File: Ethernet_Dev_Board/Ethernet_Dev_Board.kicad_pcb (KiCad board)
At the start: 2 copper layers, 123 parts, among them J102 5V, J103 3.3V, J104 3.3VA, J105 3.3VD, J401 TAG-CONNECT_NL_10-POS_LEGS, Q201 PMV48XPA2R, Q401 PMV48XPA2R, Q402 PMV48XPA2R, U101 AZ1117, U201 WIZNET_W5500, U202 74AUP1T08GWH, U302 74AUP1T08GWH, U401 74AUP1T08GWH, U402 ESP32-WROOM-32E

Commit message: Added in 1.2 V regulator and broke out unused IO pins to header
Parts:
- removed Q401, Q402: PMV48XPA2R, RG_TO_SOT_SMD:SOT23-3P95
- removed R404, R405: 10k, RG_Resistors_SMD:0603
- added J101: Power In, RG_Terminals:CUI_TBP01R1-508-02BE, F.Cu at (57.2, 49.2)
- added TVS101: 3.3V, RG_Diode:SMB-D, F.Cu at (71.8, 41.3)
- added TVS102: 3.3V, RG_Diode:SMB-D, F.Cu at (71.8, 46.6)
- added Y201: 25MHz, RG_Crystal:Crystal_SMD_4Pin_7.0mmx5.0mm, F.Cu at (47.4, 57.0)
- added Y301: 25MHz, RG_Crystal:Crystal_SMD_4Pin_3.2x2.5mm, F.Cu at (67.0, 56.0)
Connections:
- LED401 pad C: GNDS -> Net-(U402-IO16)
- LED402 pad C: GNDS -> Net-(U402-IO22)
- R406 pad 2: Net-(Q401-D) -> +3.3V
- R407 pad 2: Net-(Q402-D) -> +3.3V
- U402 pad 27: Net-(Q401-G) -> Net-(U402-IO16)
- U402 pad 36: Net-(Q402-G) -> Net-(U402-IO22)

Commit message: Net adjustments. Beginning board layout
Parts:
- removed J102: 5V, RG_Terminals:PAD_0.0638
- removed J103: 3.3V, RG_Terminals:PAD_0.0638
- removed J104: 3.3VA, RG_Terminals:PAD_0.0638
- removed J105: 3.3VD, RG_Terminals:PAD_0.0638
- added C114: 0.1uF, RG_Capacitors_SMD:0603, F.Cu at (98.6, 63.5)
- added C116: 1uF, RG_Capacitors_SMD:0603, F.Cu at (98.6, 66.1)
- added J402: ~, Connector_PinHeader_2.54mm:PinHeader_1x14_P2.54mm_Vertical, F.Cu at (111.8, 47.0)
- added R404: 10k, RG_Resistors_SMD:0603, F.Cu at (64.3, 56.8)
- added U102: 1.2V, RG_TO_SOT_SMD:SOT23-5P65, F.Cu at (97.1, 58.8)
- LED101: value 5V Power -> Power
- LED201: value ACTLED -> 5500 ACT
- LED301: value ACTLED -> 5100 ACT
- LED401: renamed from LED402; value ETH Connected -> ETH
- LED402: renamed from LED401; value MQTT Connected -> MQTT
- moved R319 132.1 mm to (50.0, 98.4), turned to 90 degrees
- moved LED301 124.1 mm to (50.5, 101.6)
- moved R405 88.1 mm to (44.5, 98.5), turned to 90 degrees
- moved R406 86.1 mm to (47.2, 98.5), turned to 90 degrees
- moved Y201 84.9 mm to (123.2, 95.2)
- moved LED402 82.5 mm to (42.2, 106.7)
- moved LED401 81.2 mm to (42.2, 104.1)
- moved C117 80.8 mm to (147.3, 88.9), turned to 180 degrees
- moved R213 79.3 mm to (138.4, 74.9)
- moved R102 77.6 mm to (138.4, 78.7), turned to 180 degrees
- moved C115 77.3 mm to (138.4, 77.5), turned to 180 degrees
- moved C207 76.0 mm to (131.2, 82.5)
- moved S401 74.6 mm to (65.4, 103.8)
- moved D301 73.8 mm to (115.0, 36.8)
- moved C403 73.5 mm to (48.0, 80.2), turned to 180 degrees
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- renumbered C114 to C115, C115 to C117, R407 to R405
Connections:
- net Net-(R302-Pad2) renamed /W5100S_Dev/TX51_N
- net Net-(R303-Pad2) renamed /W5100S_Dev/TX51_P
- net Net-(R304-Pad2) renamed /W5100S_Dev/RX51_N
- net Net-(R305-Pad2) renamed /W5100S_Dev/RX51_P
- net Net-(U301-RXIN) renamed /W5100S_Dev/RXI_N
- net Net-(U301-RXIP) renamed /W5100S_Dev/RXI_P
- net Net-(U301-TXON) renamed /W5100S_Dev/TXO_N
- net Net-(U301-TXOP) renamed /W5100S_Dev/TXO_P
- net Net-(U401A-A) renamed /ESP32/ESP_RST
- net RXN renamed RX_N
- net RXN_ETH renamed ETH_RX_N
- net RXP renamed RX_P
- net RXP_ETH renamed ETH_RX_P
- net TXN renamed TX_N
- net TXN_ETH renamed ETH_TX_N
- net TXP renamed TX_P
- net TXP_ETH renamed ETH_TX_P
- C102 pad 2: GNDS -> GND1
- C103 pad 2: GNDS -> GND1
- C105 pad 2: GNDS -> GND1
- C106 pad 2: GNDS -> GND1
- C107 pad 2: GNDS -> GND1
- C108 pad 2: GNDS -> GND1
- C109 pad 2: GNDS -> GND1
- C110 pad 2: GNDS -> GND1
- C111 pad 2: GNDS -> GND1
- C112 pad 2: GNDS -> GND1
- C113 pad 2: GNDS -> GND1
- C115 pad 2: GNDS -> GND1
- C117 pad 2: GNDS -> GND1
- C201 pad 2: GNDS -> GND1
- C202 pad 2: GNDS -> GND1
- C203 pad 2: GNDS -> GND1
- C204 pad 2: GNDS -> GND1
- C205 pad 2: GNDS -> GND1
- C206 pad 2: GNDS -> GND1
- C209 pad 2: GNDS -> GND1
- C210 pad 2: GNDS -> GND1
- C301 pad 2: GNDS -> GND1
- C302 pad 1: +1.2VO -> +1.2V
- C302 pad 2: GNDS -> GND1
- C303 pad 2: GNDS -> GND1
- C304 pad 2: GNDS -> GND1
- C305 pad 2: GNDS -> GND1
- C306 pad 2: GNDS -> GND1
- C307 pad 2: GNDS -> GND1
- C308 pad 2: GNDS -> GND1
- C309 pad 2: GNDS -> GND1
- C310 pad 2: GNDS -> GND1
- C311 pad 2: GNDS -> GND1
- C312 pad 2: GNDS -> GND1
- C313 pad 2: GNDS -> GND1
- C401 pad 2: GNDS -> GND1
- C402 pad 2: GNDS -> GND1
- C403 pad 2: GNDS -> GND1
- C404 pad 2: GNDS -> GND1
- C405 pad 2: GNDS -> GND1
- C406 pad 2: GNDS -> GND1
- J401 pad 10: GNDS -> GND1
- LED402 pad C: Net-(U402-IO16) -> Net-(U402-IO17)
- R201 pad 2: GNDS -> GND1
- R202 pad 10: GNDS -> GND1
- R204 pad 1: GNDS -> GND1
- R301 pad 1: +1.2VO -> +1.2V
- R318 pad 1: GNDS -> GND1
- S401 pad 2: GNDS -> GND1
- S401 pad 4: GNDS -> GND1
- S402 pad 2: GNDS -> GND1
- S402 pad 4: GNDS -> GND1
- TVS101 pad A: GNDS -> GND1
- TVS102 pad A: GNDS -> GND1
- U201 pad 14: GNDS -> GND1
- U201 pad 16: GNDS -> GND1
- U201 pad 19: GNDS -> GND1
- U201 pad 29: GNDS -> GND1
- U201 pad 3: GNDS -> GND1
- U201 pad 48: GNDS -> GND1
- U201 pad 9: GNDS -> GND1
- U202 pad 3: GNDS -> GND1
- U301 pad 1: GNDS -> GND1
- U301 pad 10: GNDS -> GND1
- U301 pad 23: GNDS -> GND1
- U301 pad 25: GNDS -> GND1
- U301 pad 26: GNDS -> GND1
- U301 pad 27: GNDS -> GND1
- U301 pad 28: GNDS -> GND1
- U301 pad 46: GNDS -> GND1
- U301 pad 7: GNDS -> GND1
- U302 pad 3: GNDS -> GND1
- U401 pad 3: GNDS -> GND1
- U402 pad 1: GNDS -> GND1
- U402 pad 10: unconnected-(U402-IO25-Pad10) -> IO25
- U402 pad 11: unconnected-(U402-IO26-Pad11) -> IO26
- U402 pad 12: unconnected-(U402-IO27-Pad12) -> IO27
- U402 pad 13: unconnected-(U402-IO14-Pad13) -> IO14
- U402 pad 14: unconnected-(U402-IO12-Pad14) -> IO12
- U402 pad 15: GNDS -> GND1
- U402 pad 16: unconnected-(U402-IO13-Pad16) -> IO3
- U402 pad 23: unconnected-(U402-IO15-Pad23) -> IO5
- U402 pad 24: unconnected-(U402-IO2-Pad24) -> IO2
- U402 pad 28: unconnected-(U402-IO17-Pad28) -> Net-(U402-IO17)
- U402 pad 29: unconnected-(U402-IO5-Pad29) -> IO5
- U402 pad 33: unconnected-(U402-IO21-Pad33) -> IO21
- U402 pad 38: GNDS -> GND1
- U402 pad 39: GNDS -> GND1
- U402 pad 8: unconnected-(U402-IO32-Pad8) -> IO32
- U402 pad 9: unconnected-(U402-IO33-Pad9) -> IO33
- Y201 pad 2: GNDS -> GND1
- Y301 pad 2: GNDS -> GND1
- Y301 pad 4: +1.2VO -> +1.2V

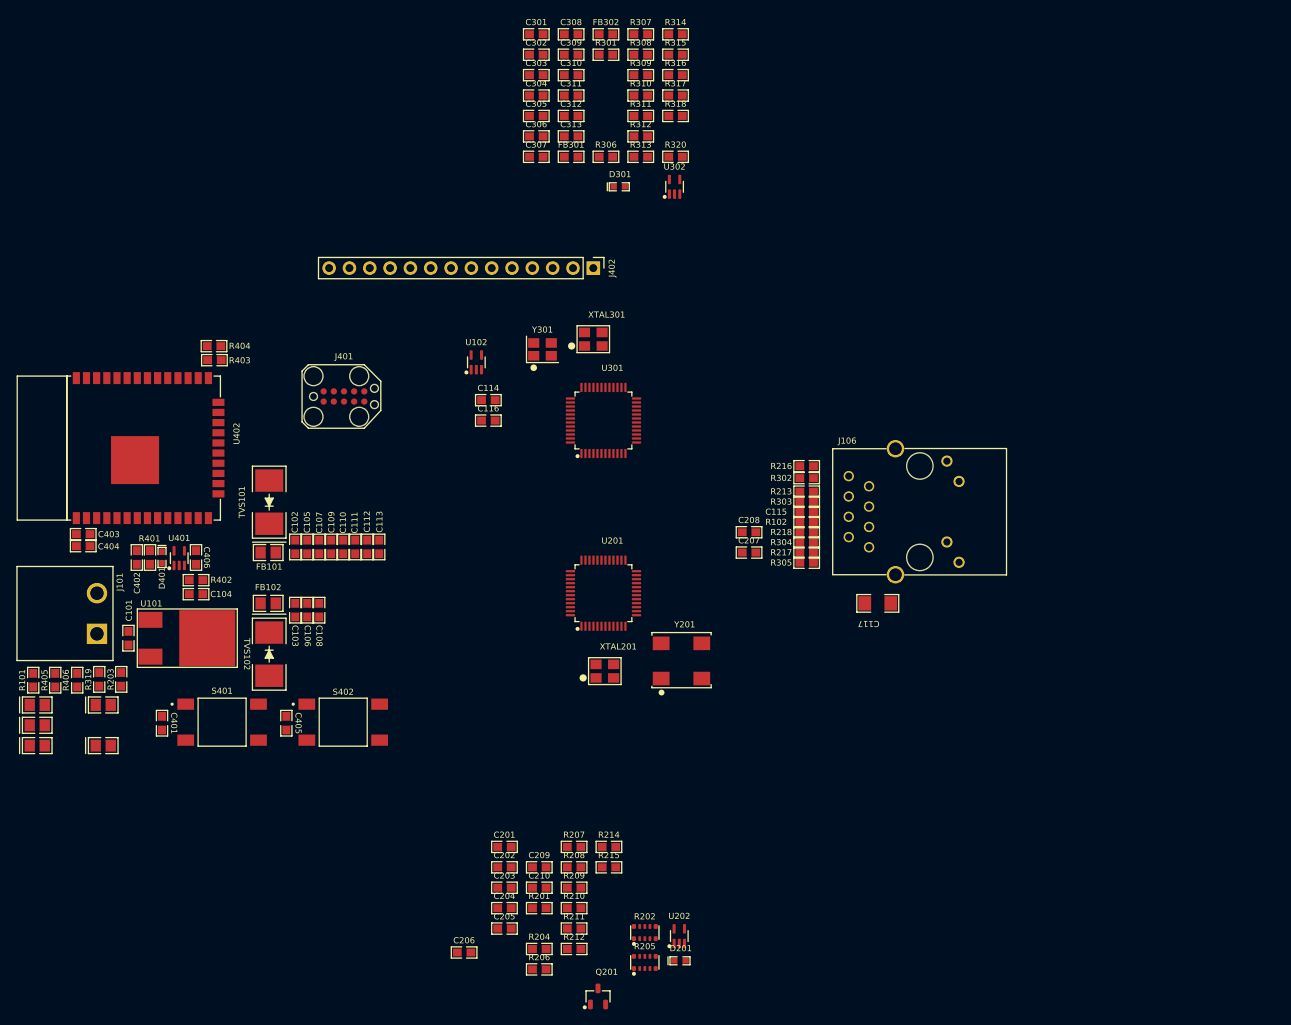
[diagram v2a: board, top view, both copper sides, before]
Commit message: Initial component placement
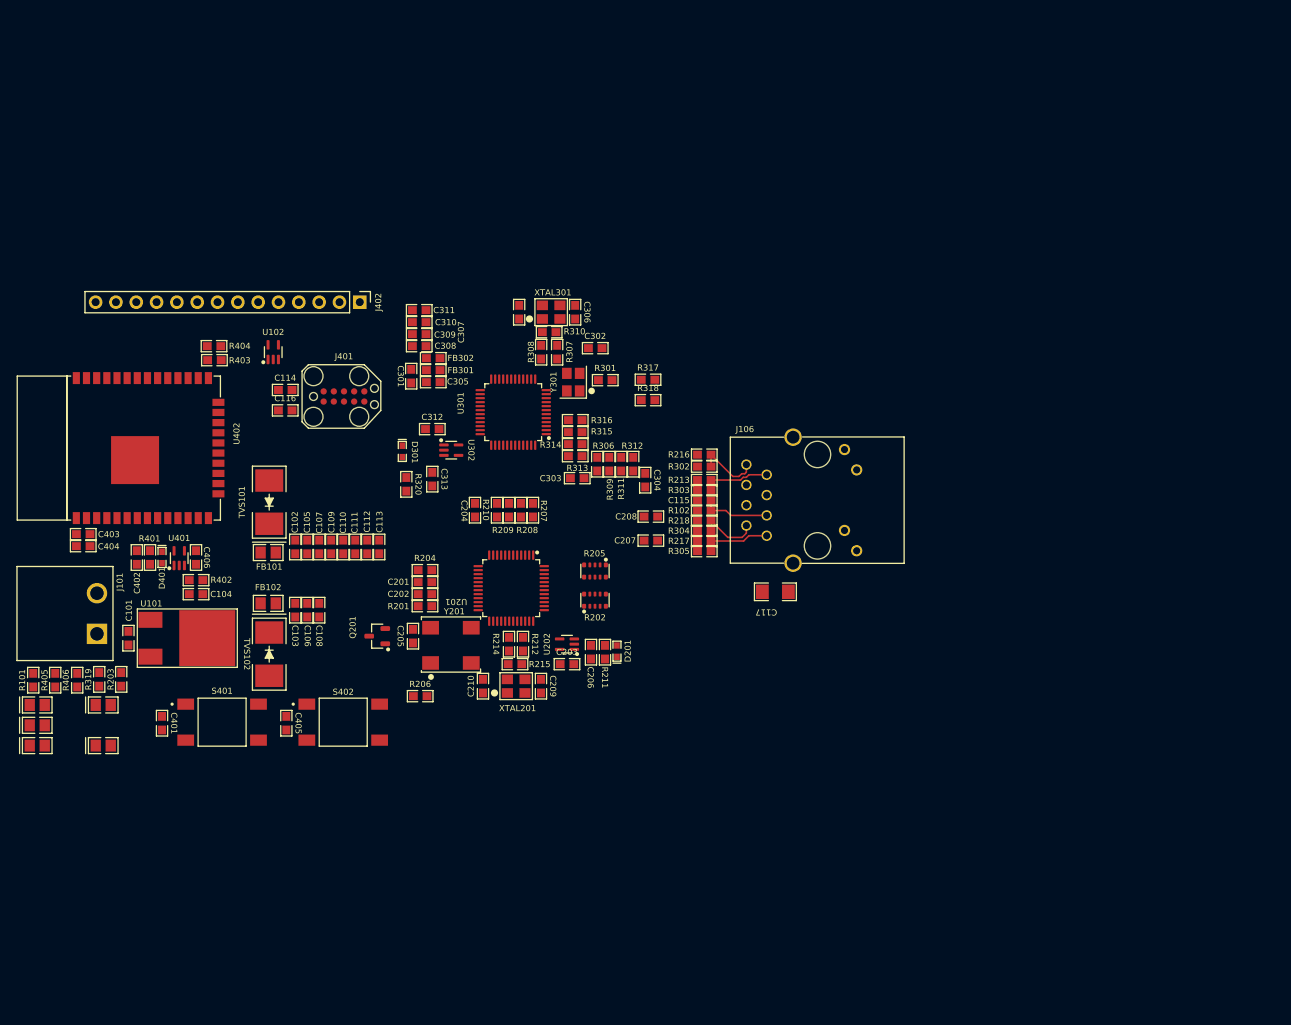
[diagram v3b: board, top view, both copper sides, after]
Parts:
- moved R320 53.0 mm to (88.4, 74.0), turned to -90 degrees
- moved Q201 52.8 mm to (84.8, 93.0), turned to 90 degrees
- moved R314 52.7 mm to (109.5, 69.0), turned to 180 degrees
- moved R210 50.7 mm to (99.7, 77.2), turned to -90 degrees
- moved C303 50.6 mm to (109.8, 73.2), turned to 180 degrees
- moved C304 50.0 mm to (118.2, 73.5), turned to -90 degrees
- moved C204 49.9 mm to (97.0, 77.2), turned to -90 degrees
- moved R204 49.5 mm to (90.7, 84.8)
- moved R205 49.3 mm to (112.0, 84.9), turned to 180 degrees
- moved R315 48.8 mm to (109.5, 67.5), turned to 180 degrees
- moved R309 48.8 mm to (113.8, 71.5), turned to 90 degrees
- moved R209 47.9 mm to (101.2, 77.2), turned to -90 degrees
- moved C313 46.2 mm to (91.6, 73.4), turned to -90 degrees
- moved FB302 45.9 mm to (91.8, 58.2), turned to 180 degrees
- moved C301 45.5 mm to (89.0, 60.5), turned to -90 degrees
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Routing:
- net ETH_RX_P: track 0.00 -> 8.50 mm
- net ETH_TX_P: track 0.00 -> 8.50 mm
- net Net-(J106-CT): track 0.00 -> 8.47 mm
- net ETH_TX_N: track 0.00 -> 8.21 mm
- net ETH_RX_N: track 0.00 -> 7.72 mm

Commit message: Removed 1 TVS diode. removed 1 reset circuit. Placed Ethernet port in both W5500 and W5100S circuits
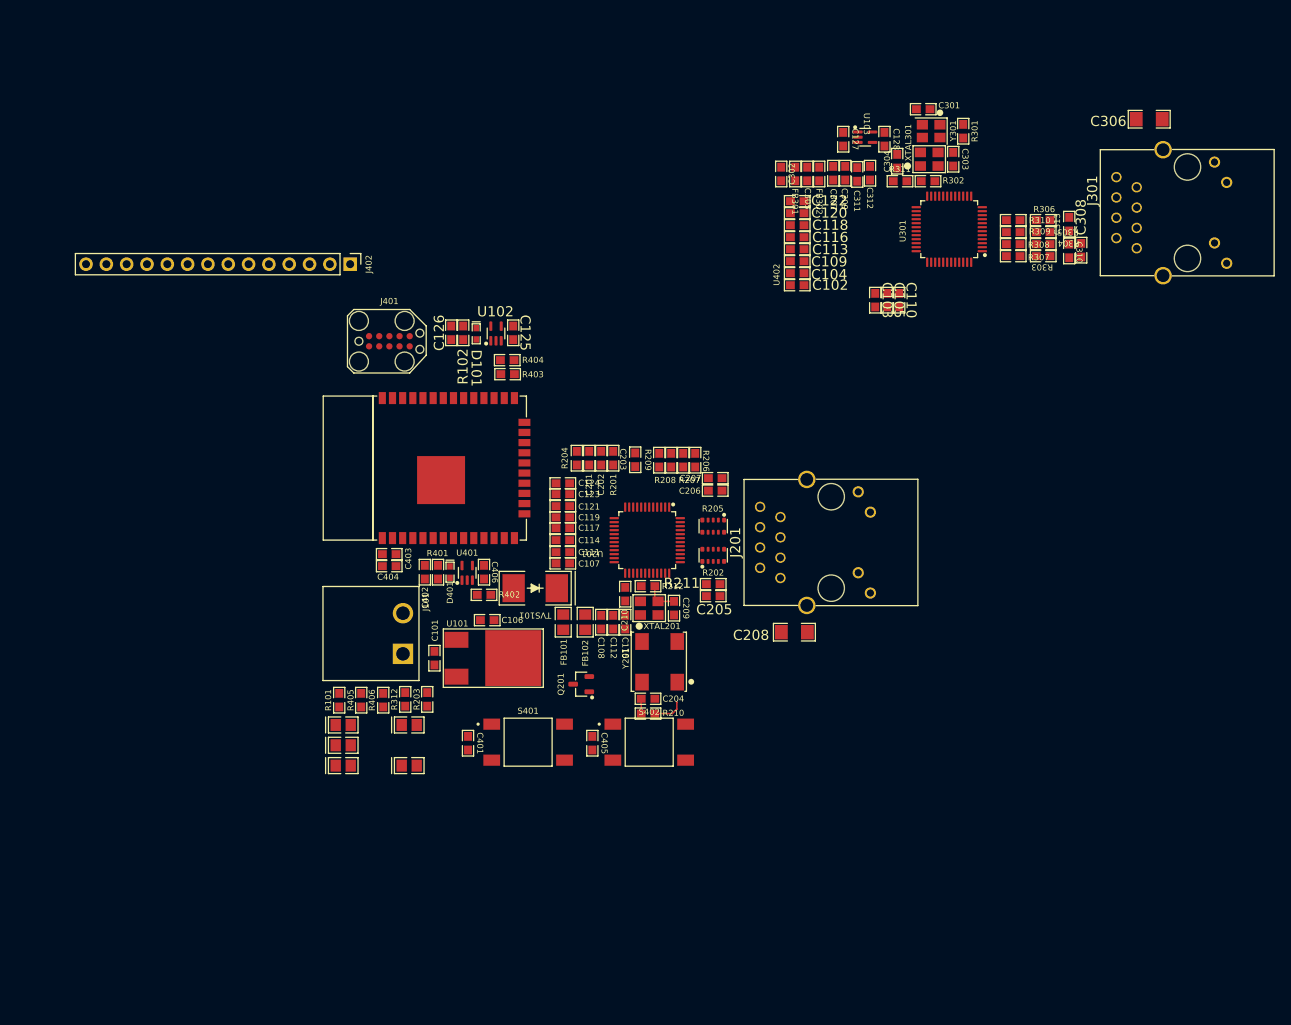
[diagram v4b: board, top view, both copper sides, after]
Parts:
- removed the C115 at (125.6, 76.0)
- removed the C117 at (134.5, 87.5)
- removed the C203 at (108.5, 96.5)
- removed the C206 at (111.5, 95.0)
- removed the C312 at (91.6, 67.1)
- removed the C313 at (91.6, 73.4)
- removed D201, D301: 1N4148X, RG_Diode:SOD-523-D
- removed J106: ~, RG_Connectors:WIZNET_RB1-125BAG1A
- removed the R212 at (103.0, 94.0)
- removed R213, R214, R216, R217, R218: 0, RG_Resistors_SMD:0603
- removed the R302 at (125.6, 71.8)
- removed the R303 at (125.6, 74.8)
- removed the R304 at (125.6, 79.8)
- removed the R305 at (125.6, 82.4)
- removed the R307 at (107.2, 57.5)
- removed the R308 at (105.2, 57.5)
- removed R318: 300, RG_Resistors_SMD:0603
- removed R320: 10k, RG_Resistors_SMD:0603
- removed TVS102: 3.3V, RG_Diode:SMB-D
- removed U202, U302: 74AUP1T08GWH, RG_TO_SOT_SMD:SOT23-5P65
- added C102: 22uF, RG_Capacitors_SMD:0603, F.Cu at (137.2, 49.1)
- added C103: 22uF, RG_Capacitors_SMD:0603, F.Cu at (147.0, 51.0)
- added C104: 22uF, RG_Capacitors_SMD:0603, F.Cu at (137.2, 47.6)
- added C105: 22uF, RG_Capacitors_SMD:0603, F.Cu at (148.5, 51.0)
- added C109: 0.1uF, RG_Capacitors_SMD:0603, F.Cu at (137.2, 46.1)
- added C110: 0.1uF, RG_Capacitors_SMD:0603, F.Cu at (150.0, 51.0)
- added C113: 0.1uF, RG_Capacitors_SMD:0603, F.Cu at (137.2, 44.6)
- added C116: 0.1uF, RG_Capacitors_SMD:0603, F.Cu at (137.2, 43.1)
- added C118: 0.1uF, RG_Capacitors_SMD:0603, F.Cu at (137.2, 41.6)
- added C120: 0.1uF, RG_Capacitors_SMD:0603, F.Cu at (137.2, 40.1)
- added C122: 0.1uF, RG_Capacitors_SMD:0603, F.Cu at (137.2, 38.6)
- added C125: 0.1uF, RG_Capacitors_SMD:0603, F.Cu at (101.8, 55.1)
- added C126: 2.2uF, RG_Capacitors_SMD:0603, F.Cu at (94.0, 55.1)
- added C205: 0.1uF, RG_Capacitors_SMD:0603, F.Cu at (126.8, 88.0)
- added C208: 1nF, RG_Capacitors_SMD:1206, F.Cu at (136.9, 92.5)
- added C306: 1nF, RG_Capacitors_SMD:1206, F.Cu at (181.2, 28.4)
- added C308: 0.1uF, RG_Capacitors_SMD:0603, F.Cu at (172.8, 44.8)
- added D101: 1N4148X, RG_Diode:SOD-523-D, F.Cu at (97.1, 55.2)
- added J201: ~, RG_Connectors:WIZNET_RB1-125BAG1A, F.Cu at (139.5, 81.3)
- added J301: ~, RG_Connectors:WIZNET_RB1-125BAG1A, F.Cu at (184.1, 40.1)
- added U102: 74AUP1T08GWH, RG_TO_SOT_SMD:SOT23-5P65, F.Cu at (99.6, 55.2)
- C209, C210: value 10pF -> 18pF
- C303: renamed from C306; value 10pF -> 18pF
- C304: renamed from C307; value 10pF -> 18pF
- R102: value 10 -> 10k
- R211: value 10k -> 10
- R311: renamed from R317; value 12k -> 12.3k
- moved C128 82.2 mm to (148.2, 30.9), turned to -90 degrees
- moved U103 78.7 mm to (145.8, 30.6), turned to -90 degrees
- moved C127 76.5 mm to (143.0, 30.9), turned to -90 degrees
- moved C310 67.7 mm to (171.2, 44.9), turned to 90 degrees
- moved C313 61.9 mm to (171.2, 41.5), turned to 90 degrees
- moved R303 61.5 mm to (168.0, 45.5), turned to 180 degrees
- moved R304 60.8 mm to (168.0, 44.0), turned to 180 degrees
- moved R305 60.2 mm to (168.0, 42.5), turned to 180 degrees
- moved R307 60.2 mm to (164.2, 45.5)
- moved R308 60.2 mm to (164.2, 44.0)
- moved R309 60.2 mm to (164.2, 42.5)
- moved R310 60.2 mm to (164.2, 41.0)
- moved R306 59.6 mm to (168.0, 41.0), turned to 180 degrees
- moved U301 59.1 mm to (156.2, 42.1)
- moved C312 58.9 mm to (146.3, 35.1), turned to 90 degrees
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- renumbered C104 to C106, C102 to C107, C103 to C108, C105 to C111, C106 to C112, C107 to C114, C108 to C115, C109 to C117, C110 to C119, C111 to C121, C112 to C123, C113 to C124, C114 to C127, C116 to C128, C204 to C203, C205 to C204, C207 to C206, C208 to C207, C302 to C301, C301 to C302, C308 to C307, C303 to C310, C310 to C311, C311 to C312, C304 to C313, R207 to R206, R208 to R207, R209 to R208, R210 to R209, R206 to R210, R215 to R212, R310 to R302, R306 to R303, R309 to R304, R311 to R305, R312 to R306, R313 to R307, R314 to R308, R315 to R309, R316 to R310, R319 to R312, U102 to U103
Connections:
- C209 pad 1: Net-(XTAL201-3@1) -> XO1
- C210 pad 1: Net-(C210-Pad1) -> XI1
- C303 pad 1: Net-(XTAL301-3@1) -> XO2
- C304 pad 1: Net-(C307-Pad1) -> XI2
- J402 pad 10: IO5 -> IO15
- R102 pad 2: +3.3VA -> +3.3V
- R211 pad 2: +3.3V -> +3.3VA
- R212 pad 1: Net-(C210-Pad1) -> XI1
- R212 pad 2: Net-(XTAL201-3@1) -> XO1
- R302 pad 1: Net-(C307-Pad1) -> XI2
- R302 pad 2: Net-(XTAL301-3@1) -> XO2
- R311 pad 1: Net-(R317-Pad1) -> GND1
- TVS101 pad C: +3.3VA -> +3.3V
- U301 pad 48: W5100_RST -> ETH_EN
- U402 pad 23: IO5 -> IO15
- XTAL201 pad 1: Net-(C210-Pad1) -> XI1
- XTAL201 pad 3: Net-(XTAL201-3@1) -> XO1
- XTAL301 pad 1: Net-(C307-Pad1) -> XI2
- XTAL301 pad 3: Net-(XTAL301-3@1) -> XO2
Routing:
- net ETH_RX_P: track 8.50 -> 0.00 mm
- net ETH_TX_P: track 8.50 -> 0.00 mm
- net Net-(U102A-C): track 8.47 -> 0.00 mm
- net ETH_TX_N: track 8.21 -> 0.00 mm
- net ETH_RX_N: track 7.72 -> 0.00 mm
- net XO1: track 0.00 -> 4.07 mm
- net Net-(Y201-OE): track 0.00 -> 3.90 mm
- net +3.3V: track 0.00 -> 1.85 mm
